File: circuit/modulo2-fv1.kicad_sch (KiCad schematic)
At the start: 82 parts, among them J1 CONN_01X04, J3 CONN_01X02, J4 HOLE, J5 HOLE, J6 USB_OTG, SW1 ROTENC_BOURNS_PEL12D, T1 B0, T2 ADC6, U1 NE5532, U10 TLE2426, U2 PWR_CONN, U3 FV-1, U4 AVR-ISP6, U5 LM1117 3V3, U6 ATmega328p, U7 DBG_UART, U8 74164, U9 AMPCTRL, Y1 12MHz

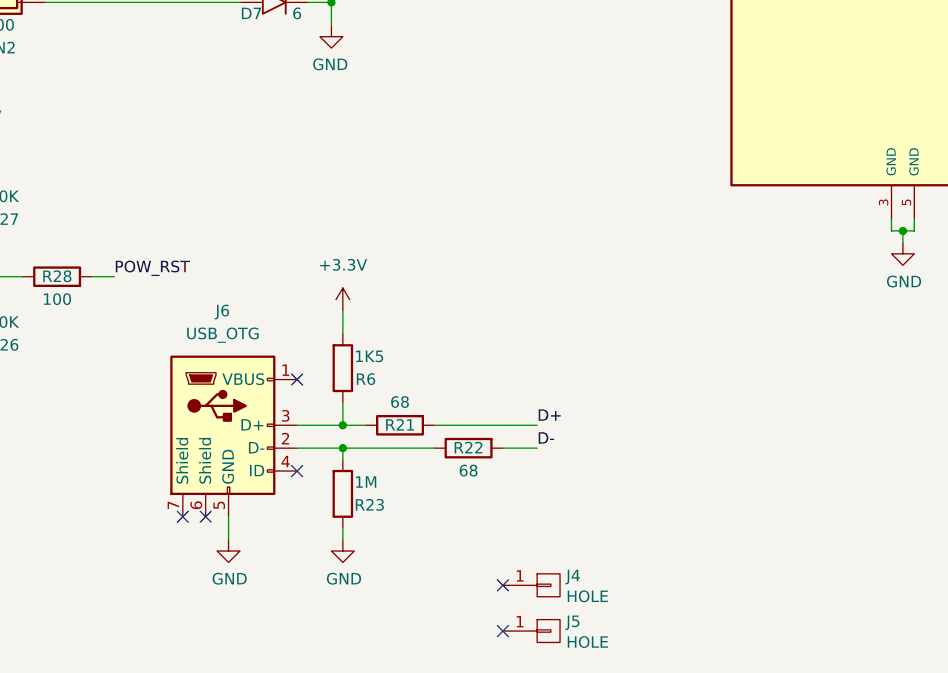
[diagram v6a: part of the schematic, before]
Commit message: fixed mistakes from assembly; added bootloader; firmware changed for PCB
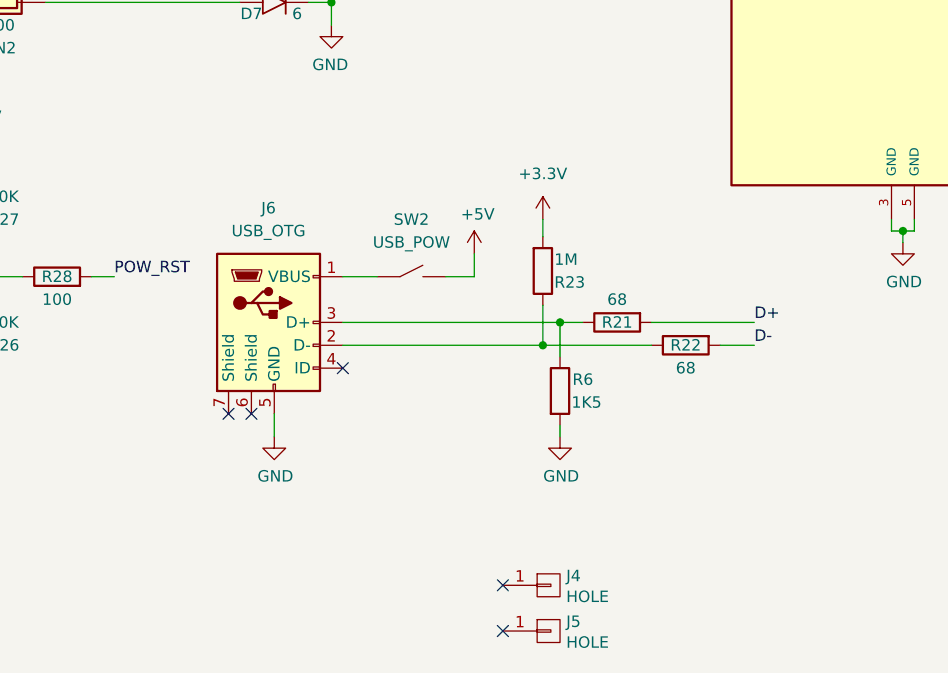
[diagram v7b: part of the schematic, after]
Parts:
- added SW2: USB_POW, myAmp:PIN_1x02, symbol myAmp:SW_SIMPLE
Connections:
- net +3V3: now also R23.2; no longer R6.2
- net +5V: now also SW2.2
- net GND: now also R6.2; no longer R23.1
- net at J6.1 (VBUS): now also SW2.1
- net at J6.2 (D-), R22.1: now also R23.1; no longer R23.2
- no-connect marks 7 -> 6
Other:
- moved on the sheet: J6, R21, R22, R23, R6
